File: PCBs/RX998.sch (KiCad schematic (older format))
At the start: 18 parts, among them J1 MIC, Q3 BC847, Q7 BF998

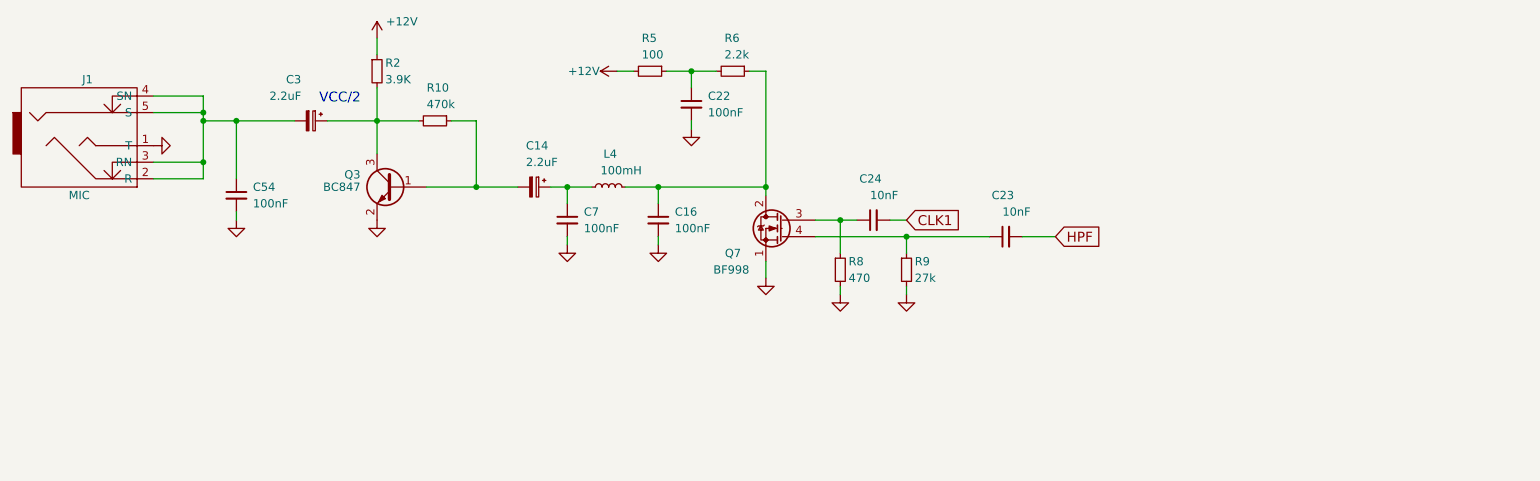
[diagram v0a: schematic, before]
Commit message: ADX988 CAT: add FE, FI commands
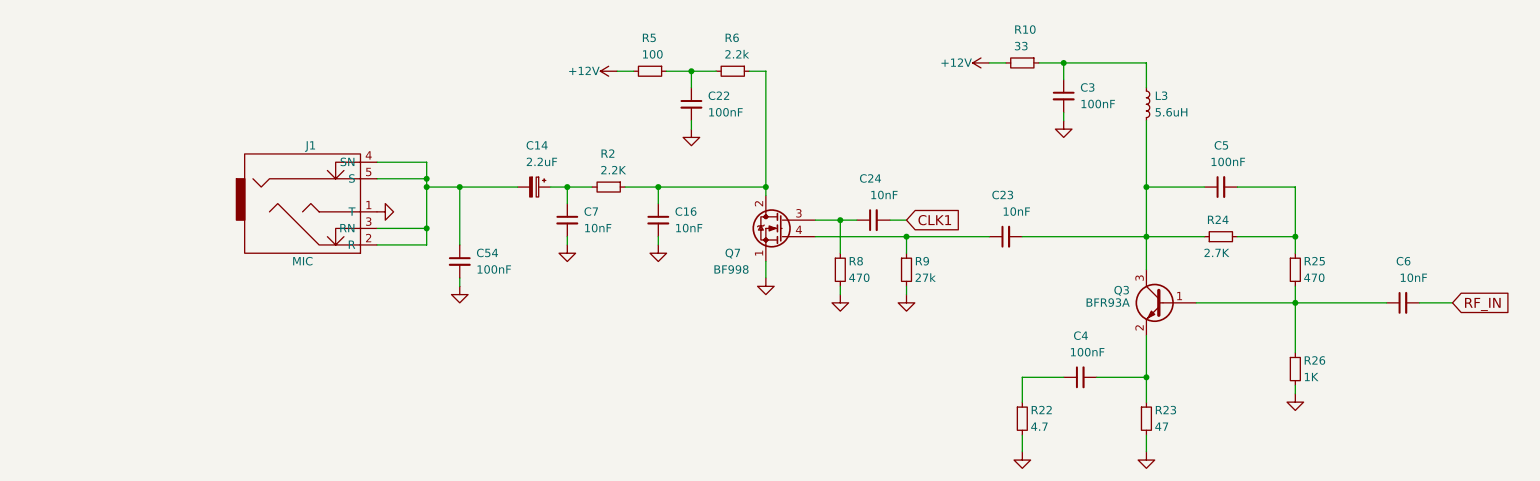
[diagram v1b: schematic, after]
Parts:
- removed C3: 2.2uF, Capacitors_THT:CP_Radial_D5.0mm_P2.00mm, symbol CP_Small
- removed L4: 100mH, Choke_Toroid_ThroughHole:Choke_Toroid_6,5x13mm_Vertical, symbol L_Small
- removed Q3: BC847, TO_SOT_Packages_SMD:SOT-23, symbol BC847
- added C3, C4, C5: 100nF, LCSDR:C_1206_0603, symbol C_Small
- added C6: 10nF, Capacitors_SMD:C_0603_HandSoldering, symbol C_Small
- added L3: 5.6uH, Choke_Axial_ThroughHole:Choke_Horizontal_RM10mm, symbol L_Small
- added Q3: BFR93A, TO_SOT_Packages_SMD:SOT-23, symbol BFR92
- added R22: 4.7, LCSDR:R_1206_0603, symbol R_Small
- added R23: 47, LCSDR:R_1206_0603, symbol R_Small
- added R24: 2.7K, LCSDR:R_1206_0603, symbol R_Small
- added R25: 470, LCSDR:R_1206_0603, symbol R_Small
- added R26: 1K, LCSDR:R_1206_0603, symbol R_Small
- C16, C7: value 100nF -> 10nF
- R10: value 470k -> 33
- R2: value 3.9K -> 2.2K
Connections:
- net +12V: now also R10.2; no longer R2.1
- net GND: now also C3.2, R22.2, R23.2, R26.2
- net at C16.1, Q7.2 (D), R6.1: now also R2.1
- net at C14.1, C7.1: now also R2.2
- net at C14.2: now also C54.1, J1.2 (R), J1.3 (RN), J1.4 (SN), J1.5 (S); no longer R10.1
- net HPF: no longer names the net of C23.2
- net HPF: now also C5.1, L3.2, Q3.3 (C), R24.1
- new net: C6.1, Q3.1 (B), R25.2, R26.1
- new net: C4.2, Q3.2 (E), R23.1
- new net: C4.1, R22.1
- new net: C5.2, R24.2, R25.1
- new net: C3.1, L3.1, R10.1
- new net RF_IN: C6.2
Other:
- note removed: "VCC/2\n"
- moved on the sheet: C54, J1
